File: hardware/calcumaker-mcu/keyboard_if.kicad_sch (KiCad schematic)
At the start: 2 parts, among them J5 TO KEYBOARD (stack), J6 TO KEYBOARD (FFC)

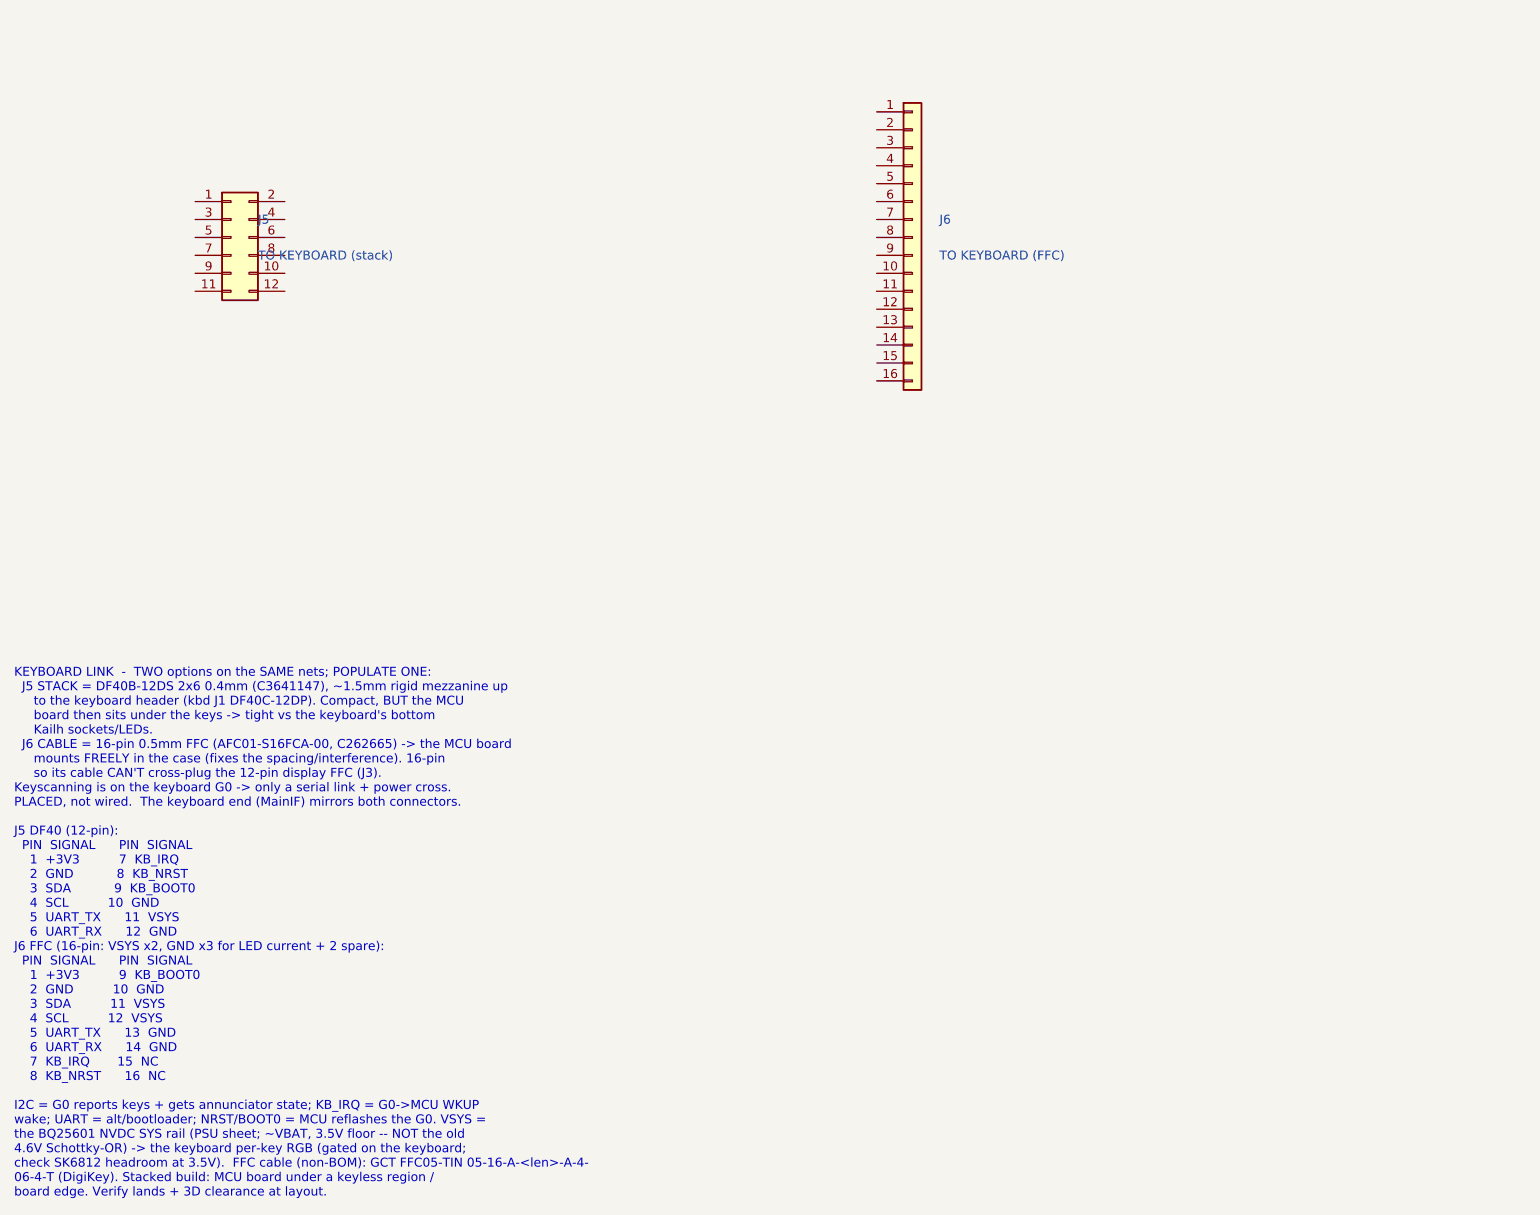
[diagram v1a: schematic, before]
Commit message: Wire mainboard and keypad schematics and verify expanded nets
Connect hierarchical interfaces, power/control circuits, debug links, matrix and RGB chains. Correct MCU package pins, diode polarity and power configuration; add bypass components and repeatable KiCad netlist/ERC checks. Document pin maps and remaining physical validation.
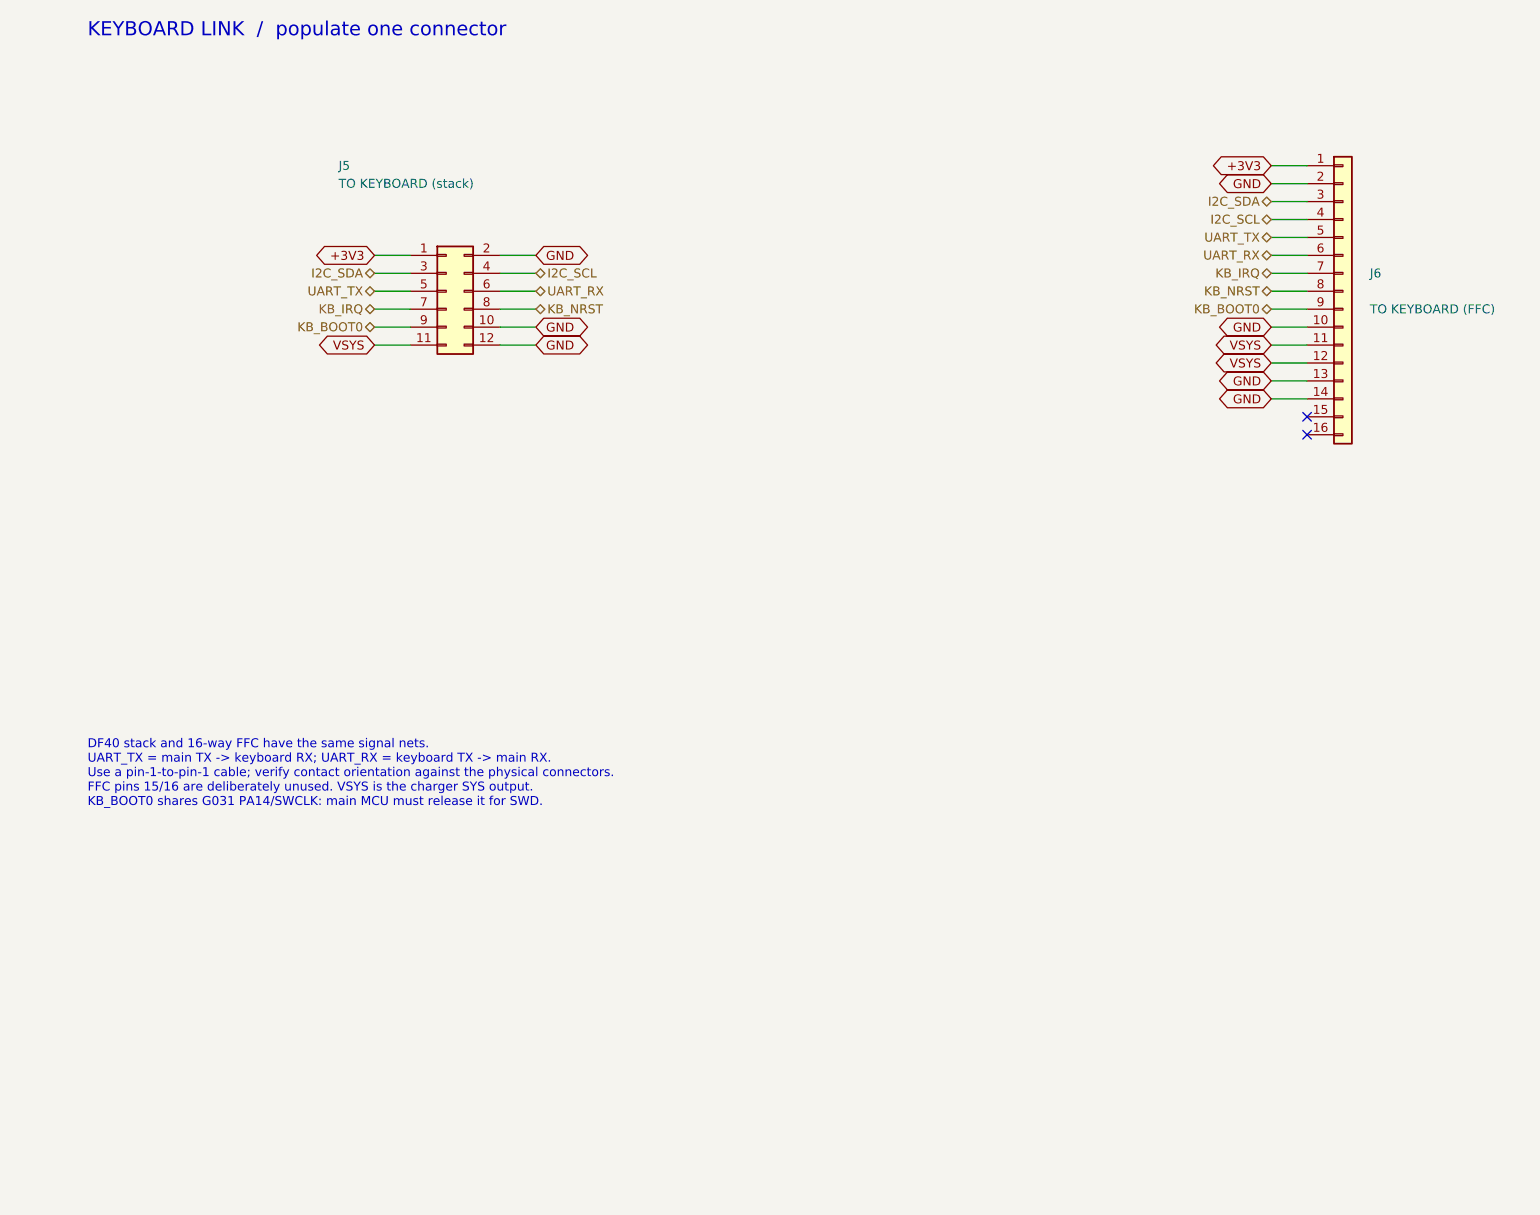
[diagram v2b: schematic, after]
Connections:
- net +3V3: now reaches J5.1 (Pin_1)
- net +3V3: now also J6.1 (Pin_1)
- net GND: now reaches J5.10 (Pin_10)
- net GND: now also J5.12 (Pin_12), J5.2 (Pin_2), J6.10 (Pin_10), J6.13 (Pin_13), J6.14 (Pin_14), J6.2 (Pin_2)
- net VSYS: now reaches J5.11 (Pin_11)
- net VSYS: now also J6.11 (Pin_11), J6.12 (Pin_12)
- net I2C_SDA: now reaches J5.3 (Pin_3)
- net I2C_SDA: now also J6.3 (Pin_3)
- net I2C_SCL: now reaches J5.4 (Pin_4)
- net I2C_SCL: now also J6.4 (Pin_4)
- net UART_TX: now reaches J5.5 (Pin_5)
- net UART_TX: now also J6.5 (Pin_5)
- net UART_RX: now reaches J5.6 (Pin_6)
- net UART_RX: now also J6.6 (Pin_6)
- net KB_IRQ: now reaches J5.7 (Pin_7)
- net KB_IRQ: now also J6.7 (Pin_7)
- net KB_NRST: now reaches J5.8 (Pin_8)
- net KB_NRST: now also J6.8 (Pin_8)
- net KB_BOOT0: now reaches J5.9 (Pin_9)
- net KB_BOOT0: now also J6.9 (Pin_9)
- no-connect marks 0 -> 2
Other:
- note added: "DF40 stack and 16-way FFC have the same signal nets. UART_TX = main TX -> keyboard RX; UART_RX = keyboard TX -> main RX. Use a pin-1-to-pin-1 cable; verify contact orientation against the physical connectors. FFC pins 15/16 are deliberately unused. VSYS is the charger SYS output. KB_BOOT0 shares G031 PA14/SWCLK: main MCU must release it for SWD."
- note added: "KEYBOARD LINK / populate one connector"
- note removed: "KEYBOARD LINK - TWO options on the SAME nets; POPULATE ONE: J5 STACK = DF40B-12DS 2x6 0.4mm (C3641147), ~1.5mm rigid mezzanine up to the keyboard header (kbd J1 DF40C-12DP). Compact, BUT the MCU board then sits under the keys -> tight vs the keyboard's bottom Kailh sockets/LEDs. J6 CABLE = 16-pin 0.5mm FFC (AFC01-S16FCA-00, C262665) -> the MCU board mounts FREELY in the case (fixes the spacing/in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"
- title: Calcumaker 16 — MCU — Keyboard link -- DF40 stack (J5) OR 16-pin FFC cable (J6), populate one -> Calcumaker 16 / mcu / keyboard if
- moved on the sheet: J5, J6
